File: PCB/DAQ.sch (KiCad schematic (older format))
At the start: 58 parts, among them IC1 MAX743CWE+, J1 Arduino_Mega_Header, J10 Conn_01x01, J11 Conn_01x01, J12 Conn_01x01, J2 Conn_01x07, J3 Conn_01x08, J4 Conn_01x08, J5 Conn_02x18_Counter_Clockwise, J6 Conn_01x10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

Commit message: PCB Upgraded and screens of the DAC analog
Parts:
- removed J10, J11, J12, J9: Conn_01x01, Pin_Headers:Pin_Header_Straight_1x01_Pitch2.54mm, symbol Conn_01x01
- added C9: 100nF, Resistors_THT:R_Axial_DIN0204_L3.6mm_D1.6mm_P7.62mm_Horizontal, symbol C
- added R19: 270k, Resistors_THT:R_Axial_DIN0207_L6.3mm_D2.5mm_P7.62mm_Horizontal, symbol R
- R7: value 47 -> 47k
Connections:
- net 15V is gone; now on net +15V: C5.2, C8.2, R3.1, U6.8 (V+), U6.8 (V+), U7.8 (V+)
- net GND: now also C9.2
- net VinADC: now reaches U3.8 (A1)
- net VinADC: now also R8.1, U7.1
- net Vo renamed VoDAC1
- net VoDAC1: now also R19.2
- new net VoDAC: C9.1, R19.1
- no-connect marks 132 -> 131
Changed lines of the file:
@@
-$EndComp
-$Comp
-L ADC U3
-U 1 1 5AA58804
-P 3650 3600
-F 0 "U3" H 4050 3050 60  0000 C CNN
-F 1 "ADC" H 4250 3050 60  0000 C CNN
-F 2 "ADC:ADC" H 5000 3500 60  0001 C CNN
-F 3 "" H 5000 3500 60  0001 C CNN
-	1    3650 3600
-	0    -1   -1   0
 $EndComp
 $Comp
@@
 NoConn ~ 3450 3100
 NoConn ~ 3450 3200
-NoConn ~ 3450 3400
 NoConn ~ 3450 3300
 NoConn ~ 3450 3500
@@
 P 3900 7550
 F 0 "R7" V 3980 7550 50  0000 C CNN
-F 1 "47" V 3900 7550 50  0000 C CNN
+F 1 "47k" V 3900 7550 50  0000 C CNN
 F 2 "Resistors_THT:R_Axial_DIN0207_L6.3mm_D2.5mm_P7.62mm_Horizontal" V 3830 7550 50  0001 C CNN
 F 3 "" H 3900 7550 50  0001 C CNN
@@
 $EndComp
 Text Label 3050 7050 0    39   ~ 0
-15V
++15V
 Text Label 1300 5800 0    39   ~ 0
-15V
++15V
 Text Label 1300 6400 0    39   ~ 0
 -15V
@@
 $EndComp
 Text Label 2450 6150 0    39   ~ 0
-15V
++15V
 Text Label 2750 6300 0    39   ~ 0
 GND
 Text Label 4100 6200 0    39   ~ 0
-15V
++15V
 Text Label 4400 6300 0    39   ~ 0
 GND
@@
 SDA
 $Comp
-L Conn_01x01 J11
-U 1 1 5AC6A77C
-P 4450 4600
-F 0 "J11" H 4450 4700 50  0000 C CNN
-F 1 "Conn_01x01" H 4450 4500 50  0000 C CNN
-F 2 "Pin_Headers:Pin_Header_Straight_1x01_Pitch2.54mm" H 4450 4600 50  0001 C CNN
-F 3 "" H 4450 4600 50  0001 C CNN
-	1    4450 4600
-	1    0    0    -1
-$EndComp
-$Comp
-L Conn_01x01 J12
-U 1 1 5AC6A7F5
-P 4450 4900
-F 0 "J12" H 4450 5000 50  0000 C CNN
-F 1 "Conn_01x01" H 4450 4800 50  0000 C CNN
-F 2 "Pin_Headers:Pin_Header_Straight_1x01_Pitch2.54mm" H 4450 4900 50  0001 C CNN
-F 3 "" H 4450 4900 50  0001 C CNN
-	1    4450 4900
-	1    0    0    -1
-$EndComp
-$Comp
-L Conn_01x01 J9
-U 1 1 5AC6A961
-P 3800 4900
-F 0 "J9" H 3800 5000 50  0000 C CNN
-F 1 "Conn_01x01" H 3800 4800 50  0000 C CNN
-F 2 "Pin_Headers:Pin_Header_Straight_1x01_Pitch2.54mm" H 3800 4900 50  0001 C CNN
-F 3 "" H 3800 4900 50  0001 C CNN
-	1    3800 4900
-	1    0    0    -1
-$EndComp
-$Comp
-L Conn_01x01 J10
-U 1 1 5AC6A967
-P 3800 5200
-F 0 "J10" H 3800 5300 50  0000 C CNN
-F 1 "Conn_01x01" H 3800 5100 50  0000 C CNN
-F 2 "Pin_Headers:Pin_Header_Straight_1x01_Pitch2.54mm" H 3800 5200 50  0001 C CNN
-F 3 "" H 3800 5200 50  0001 C CNN
-	1    3800 5200
-	1    0    0    -1
-$EndComp
-Text Label 3600 4900 2    39   ~ 0
-PIN50
-Text Label 4250 4600 2    39   ~ 0
-PIN50
-Text Label 4250 4900 2    39   ~ 0
-PIN52
-Text Label 3600 5200 2    39   ~ 0
-PIN52
-$Comp
 L LM358 U8
 U 1 1 5ACCFE80
@@
 Text Label 10250 5950 0    39   ~ 0
 GND
-Text Label 11100 5150 0    39   ~ 0
-Vo
 Text Label 8600 5350 0    60   ~ 0
 -15V
@@
 Text Label 8200 6250 0    39   ~ 0
 GND
+Wire Wire Line
+	4500 6900 4750 6900
+Text Label 4750 6900 0    60   ~ 0
+VinADC
+$Comp
+L ADC U3
+U 1 1 5AA58804
+P 3650 3600
+F 0 "U3" H 4050 3050 60  0000 C CNN
+F 1 "ADC" H 4250 3050 60  0000 C CNN
+F 2 "ADC:ADC" H 5000 3500 60  0001 C CNN
+F 3 "" H 5000 3500 60  0001 C CNN
+	1    3650 3600
+	0    -1   -1   0
+$EndComp
+Text Label 3450 3400 2    39   ~ 0
+VinADC
+$Comp
+L R R19
+U 1 1 5AD7CDA2
+P 9000 3900
+F 0 "R19" V 9080 3900 50  0000 C CNN
+F 1 "270k" V 9000 3900 50  0000 C CNN
+F 2 "Resistors_THT:R_Axial_DIN0207_L6.3mm_D2.5mm_P7.62mm_Horizontal" V 8930 3900 50  0001 C CNN
+F 3 "" H 9000 3900 50  0001 C CNN
+	1    9000 3900
+	0    1    1    0
+$EndComp
+$Comp
+L C C9
+U 1 1 5AD7CE41
+P 9350 4050
+F 0 "C9" H 9375 4150 50  0000 L CNN
+F 1 "100nF" H 9375 3950 50  0000 L CNN
+F 2 "Resistors_THT:R_Axial_DIN0204_L3.6mm_D1.6mm_P7.62mm_Horizontal" H 9388 3900 50  0001 C CNN
+F 3 "" H 9350 4050 50  0001 C CNN
+	1    9350 4050
+	1    0    0    -1
+$EndComp
+Wire Wire Line
+	9150 3900 9500 3900
+Text Label 11100 5150 0    39   ~ 0
+VoDAC1
+Text Label 8850 3900 2    39   ~ 0
+VoDAC1
+Text Label 9350 4200 2    39   ~ 0
+GND
+Connection ~ 9350 3900
+Text Label 9500 3900 0    39   ~ 0
+VoDAC
 $EndSCHEMATC

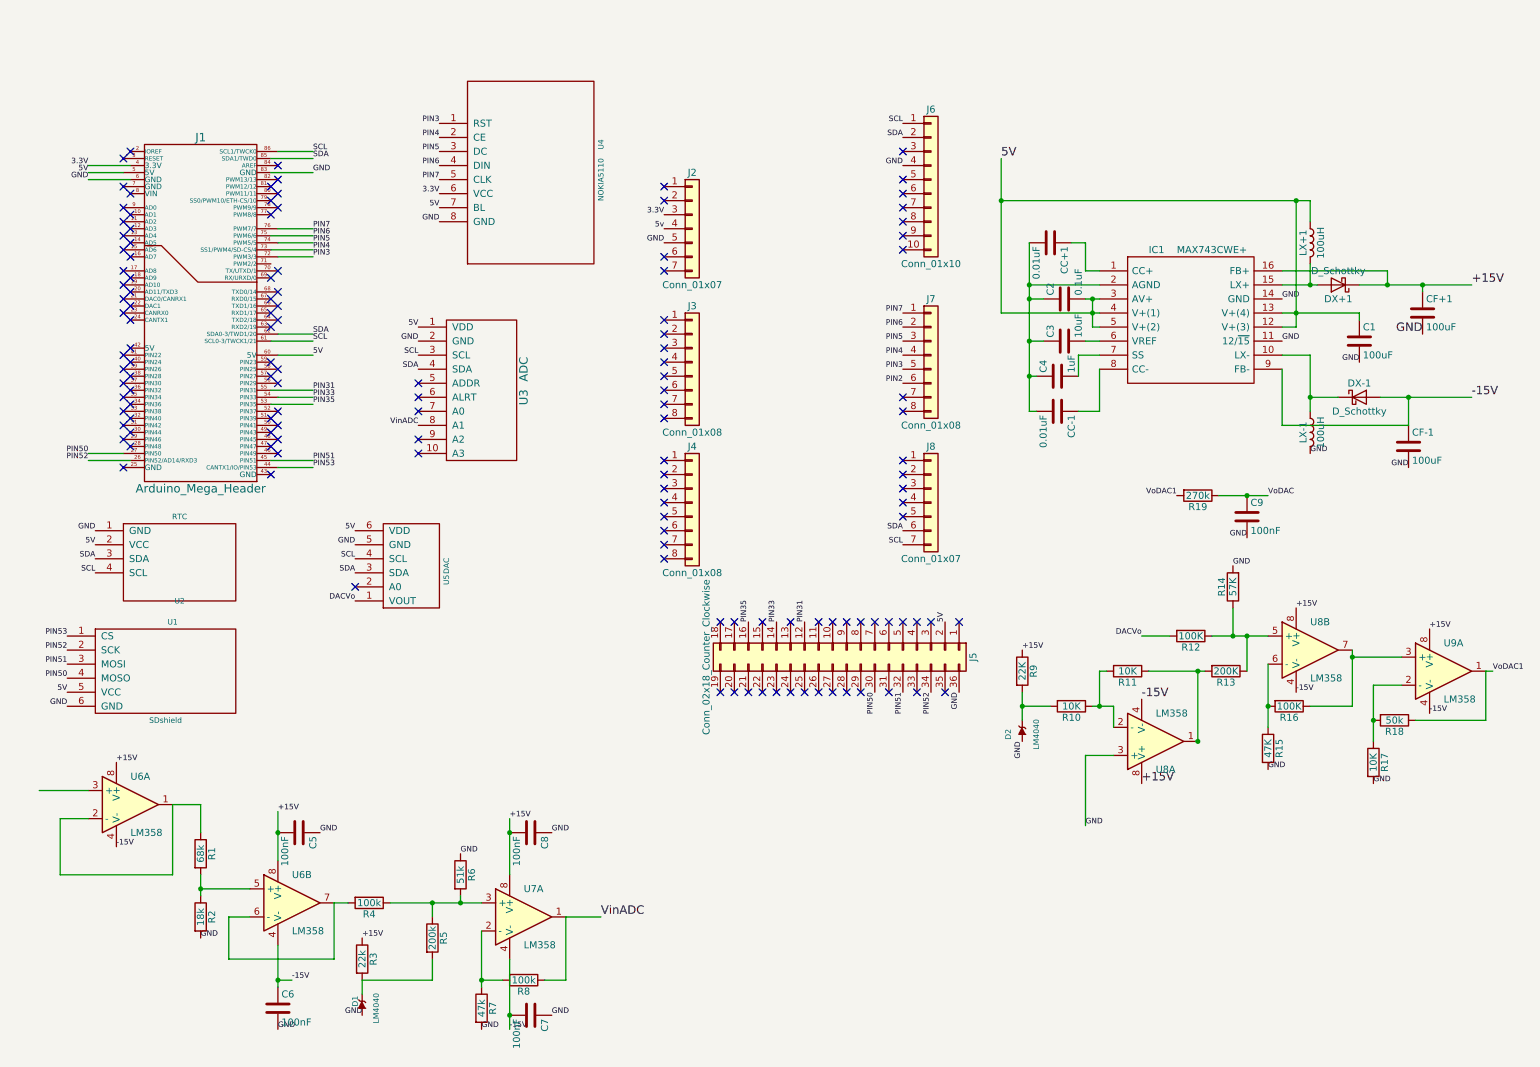
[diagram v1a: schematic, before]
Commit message: Code modulation and PCB improvements. Multiplexer added
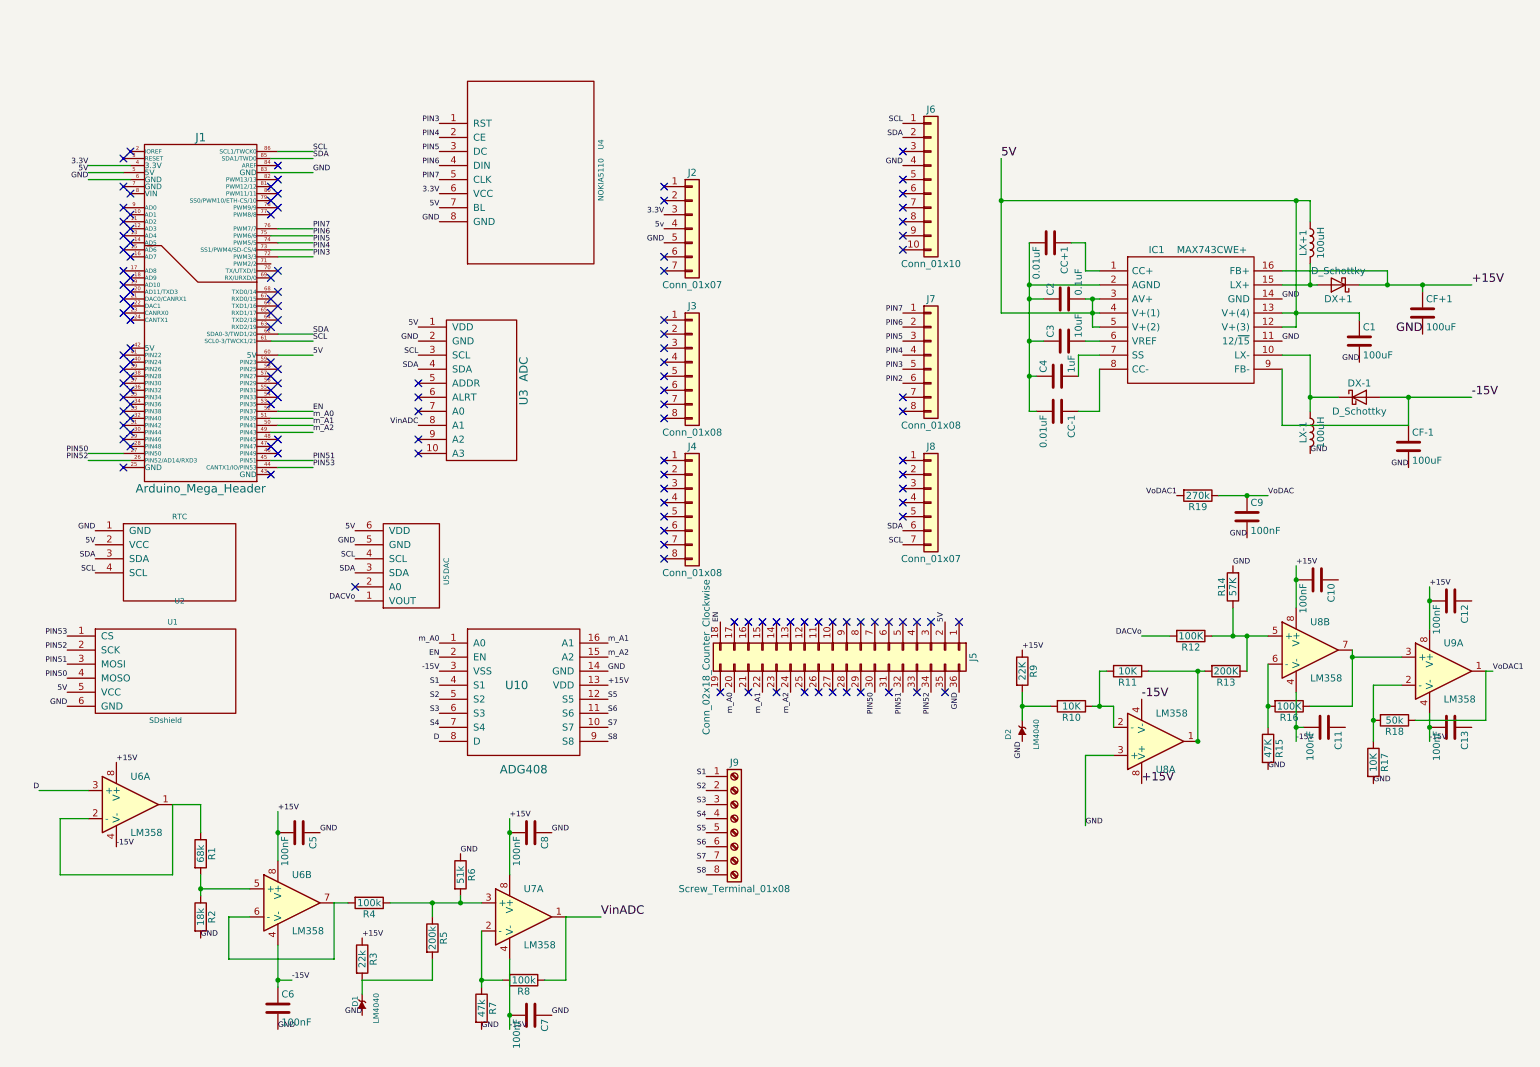
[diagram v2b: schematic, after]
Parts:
- added C10, C11, C12, C13: 100nF, Resistors_THT:R_Axial_DIN0207_L6.3mm_D2.5mm_P7.62mm_Horizontal, symbol C
- added J9: Screw_Terminal_01x08, symbol Screw_Terminal_01x08
- added U10: ADG408, Housings_DIP:DIP-16_W7.62mm, symbol ADG408
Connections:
- net +15V: now also C10.2, C12.2, U10.13 (VDD)
- net -15V: now also C11.2, C13.2, U10.3 (VSS)
- net GND: now also U10.14 (GND)
- net m_A2: now reaches J1.49 (PIN43)
- net m_A2: now also J5.24 (Pin_24), U10.15 (A2)
- net m_A1: now reaches J1.50 (PIN41)
- net m_A1: now also J5.22 (Pin_22), U10.16 (A1)
- net m_A0: now reaches J1.51 (PIN39)
- net m_A0: now also J5.20 (Pin_20), U10.1 (A0)
- net EN: now reaches J1.52 (PIN37)
- net EN: now also J5.18 (Pin_18), U10.2 (EN)
- net D: now reaches U6.3 (+)
- net D: now also U10.8 (D)
- net PIN31: no longer names the net of J1.55 (PIN31)
- net PIN31: no longer J5.12 (Pin_12)
- net PIN33: no longer names the net of J1.54 (PIN33)
- net PIN33: no longer J5.14 (Pin_14)
- net PIN35: no longer names the net of J1.53 (PIN35)
- net PIN35: no longer J5.16 (Pin_16)
- new net S1: J9.1 (Pin_1), U10.4 (S1)
- new net S2: J9.2 (Pin_2), U10.5 (S2)
- new net S3: J9.3 (Pin_3), U10.6 (S3)
- new net S4: J9.4 (Pin_4), U10.7 (S4)
- new net S5: J9.5 (Pin_5), U10.12 (S5)
- new net S6: J9.6 (Pin_6), U10.11 (S6)
- new net S7: J9.7 (Pin_7), U10.10 (S7)
- new net S8: J9.8 (Pin_8), U10.9 (S8)
- no-connect marks 131 -> 129

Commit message: Start of LaTeX proyect and few improvements
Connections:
- net GND: now also C10.1, C11.1, C12.1, C13.1
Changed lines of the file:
@@
 Text Label 6100 5300 3    39   ~ 0
 m_A2
+Text Label 10000 4500 0    39   ~ 0
+GND
+Text Label 10950 4650 0    39   ~ 0
+GND
+Text Label 10950 5550 0    39   ~ 0
+GND
+Text Label 10050 5550 0    39   ~ 0
+GND
 $EndSCHEMATC

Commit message: New version of PCB
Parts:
- added C?: 100nF, symbol C
- added R? (x3): R, symbol R
- added U?: LM358, symbol LM358
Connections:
- net 5V: now also R?.2, U?.4 (V-)
- net GND: now also C?.1, R?.2; no longer U8.3 (+)
- net VoDAC1: no longer R19.2
- net ARDU-A7: now reaches J1.16 (AD7)
- net ARDU-A7: now also J1.17 (AD8)
- net ARDU-A8: now reaches J1.18 (AD9)
- net ARDU-A9: now reaches J1.19 (AD10)
- net ARDU-A10: now reaches J1.20 (AD11/TXD3)
- net ADC-A3: now reaches U3.10 (A3)
- net SMU_OUT: now reaches U3.7 (A0)
- net SMU_OUT: now also R?.1, U?.1
- net ADC-A2: now reaches U3.9 (A2)
- net at R16.1, U8.7: now also R19.2; no longer U9.3 (+)
- net at R12.1, R13.1, R14.1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: now also C?.2
- net VoDAC: no longer names the net of C9.1, R19.1
- net VoDAC: now also U9.3 (+)
- new net: R?.2, U?.2 (-)
- new net: R?.1, R?.1, U?.3 (+)
- no-connect marks 129 -> 121
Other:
- moved on the sheet: C1, C10, C11, C2, C3, C4, C9, CC+1, CC-1, CF+1, CF-1, D2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
